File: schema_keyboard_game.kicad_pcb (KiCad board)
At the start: 2 copper layers, 228 parts, among them J1 USB_C_Receptacle_PowerOnly_6P, SW101 SW_Push, U1 ESP32-S3-DevKitC

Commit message: Add new layout, update schema
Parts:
- added J2: Conn_01x04, Connector_PinSocket_2.54mm:PinSocket_1x04_P2.54mm_Vertical, F.Cu at (382.3, 278.1)
- SW1, SW10, SW100, SW11, SW12, SW13, SW14, SW15, SW16, SW17, SW18, SW19, SW2, SW20, SW21, SW22, SW23, SW24, SW25, SW26, SW27, SW28, SW29, SW3, SW30, SW31, SW32, SW33, SW34, SW35, SW36, SW37, SW38, SW39, SW4, SW40, SW41, SW42, SW43, SW44, SW45, SW46, SW47, SW48, SW49, SW5, SW50, SW51, SW52, SW53, SW54, SW55, SW56, SW57, SW58, SW59, SW6, SW60, SW61, SW62, SW63, SW64, SW65, SW66, SW67, SW68, SW69, SW7, SW70, SW71, SW72, SW73, SW74, SW75, SW76, SW77, SW78, SW79, SW8, SW80, SW81, SW82, SW83, SW84, SW85, SW86, SW87, SW88, SW89, SW9, SW90, SW91, SW92, SW93, SW94, SW95, SW96, SW97, SW98, SW99: footprint Library:SW_Cherry_MX_LED -> Library:SW_Cherry_MX_LED_2
- moved SW99 30.4 mm to (232.9, 268.6)
- moved SW89 28.9 mm to (232.9, 249.4)
- moved SW79 27.6 mm to (232.9, 230.3)
- moved SW69 26.3 mm to (232.9, 211.2)
- moved SW59 25.1 mm to (232.9, 192.1)
- moved SW49 24.0 mm to (232.9, 172.9)
- moved SW80 23.9 mm to (252.7, 230.4)
- moved SW39 23.1 mm to (232.9, 153.8)
- moved SW70 22.4 mm to (252.7, 211.2)
- moved SW29 22.3 mm to (232.9, 134.7)
- moved SW19 21.7 mm to (232.9, 115.6)
- moved SW9 21.2 mm to (232.9, 96.4)
- moved SW60 21.0 mm to (252.7, 192.1)
- moved SW90 20.4 mm to (252.7, 249.5)
- moved SW50 19.7 mm to (252.7, 173.0)
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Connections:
- LCD1 pad 1: +3V3 -> GND
- LCD1 pad 2: (no net) -> +3V3

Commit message: New draft of pcb plate
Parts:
- moved SW6 123.6 mm to (34.3, 130.8)
- moved SW5 104.5 mm to (34.3, 110.5)
- moved SW21 98.8 mm to (74.9, 29.2)
- moved SW4 88.5 mm to (34.3, 90.2)
- moved SW11 85.6 mm to (54.6, 29.2)
- moved SW1 79.0 mm to (34.3, 29.2)
- moved SW3 77.6 mm to (34.3, 69.8)
- moved SW2 74.1 mm to (34.3, 49.5)
- moved SW12 8.03 mm to (95.0, 119.3)
- moved SW13 8.03 mm to (110.0, 119.3)
- moved SW22 8.03 mm to (95.0, 135.6)
- moved SW23 8.03 mm to (110.0, 135.6)
- moved SW31 8.03 mm to (79.9, 151.9)
- moved SW32 8.03 mm to (95.0, 151.9)
- moved SW33 8.03 mm to (110.0, 151.9)
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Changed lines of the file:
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@@
 	(footprint "Library:SW_Cherry_MX_LED_2"
 		(layer "F.Cu")
-		(at 77.32 176.825)
+		(at 79.86 184.445)
 		(descr "Cherry MX keyswitch, 1.00u, plate mount, http://cherryamericas.com/wp-content/uploads/2014/12/mx_cat.pdf")
 		(tags "Cherry MX keyswitch 1.00u plate")
@@
 	(footprint "Library:SW_Cherry_MX_LED_2"
 		(layer "F.Cu")
-		(at 92.41 209.375)
+		(at 94.95 216.995)
 		(descr "Cherry MX keyswitch, 1.00u, plate mount, http://cherryamericas.com/wp-content/uploads/2014/12/mx_cat.pdf")
 		(tags "Cherry MX keyswitch 1.00u plate")
@@
 	(footprint "Library:SW_Cherry_MX_LED_2"
 		(layer "F.Cu")
-		(at 92.41 225.65)
+		(at 94.95 233.27)
 		(descr "Cherry MX keyswitch, 1.00u, plate mount, http://cherryamericas.com/wp-content/uploads/2014/12/mx_cat.pdf")
 		(tags "Cherry MX keyswitch 1.00u plate")
@@
 	(footprint "Library:SW_Cherry_MX_LED_2"
 		(layer "F.Cu")
-		(at 107.5 209.375)
+		(at 110.04 216.995)
 		(descr "Cherry MX keyswitch, 1.00u, plate mount, http://cherryamericas.com/wp-content/uploads/2014/12/mx_cat.pdf")
 		(tags "Cherry MX keyswitch 1.00u plate")
@@
 	(footprint "Library:SW_Cherry_MX_LED_2"
 		(layer "F.Cu")
-		(at 77.32 225.65)
+		(at 79.86 233.27)
 		(descr "Cherry MX keyswitch, 1.00u, plate mount, http://cherryamericas.com/wp-content/uploads/2014/12/mx_cat.pdf")
 		(tags "Cherry MX keyswitch 1.00u plate")
@@
 	(footprint "Library:SW_Cherry_MX_LED_2"
 		(layer "F.Cu")
-		(at 92.41 111.725)
+		(at 94.95 119.345)
 		(descr "Cherry MX keyswitch, 1.00u, plate mount, http://cherryamericas.com/wp-content/uploads/2014/12/mx_cat.pdf")
 		(tags "Cherry MX keyswitch 1.00u plate")
@@
 	)
 	(footprint "Library:SW_Cherry_MX_LED_2"
+		(locked yes)
 		(layer "F.Cu")
-		(at 92.41 95.45)
+		(at 34.29 49.53)
 		(descr "Cherry MX keyswitch, 1.00u, plate mount, http://cherryamericas.com/wp-content/uploads/2014/12/mx_cat.pdf")
 		(tags "Cherry MX keyswitch 1.00u plate")
@@
 	(footprint "Library:SW_Cherry_MX_LED_2"
 		(layer "F.Cu")
-		(at 107.5 144.275)
+		(at 110.04 151.895)
 		(descr "Cherry MX keyswitch, 1.00u, plate mount, http://cherryamericas.com/wp-content/uploads/2014/12/mx_cat.pdf")
 		(tags "Cherry MX keyswitch 1.00u plate")
@@
 	(footprint "Library:SW_Cherry_MX_LED_2"
 		(layer "F.Cu")
-		(at 92.41 241.925)
+		(at 94.95 249.545)
 		(descr "Cherry MX keyswitch, 1.00u, plate mount, http://cherryamericas.com/wp-content/uploads/2014/12/mx_cat.pdf")
 		(tags "Cherry MX keyswitch 1.00u plate")
@@
 	(footprint "Library:SW_Cherry_MX_LED_2"
 		(layer "F.Cu")
-		(at 107.5 176.825)
+		(at 110.04 184.445)
 		(descr "Cherry MX keyswitch, 1.00u, plate mount, http://cherryamericas.com/wp-content/uploads/2014/12/mx_cat.pdf")
 		(tags "Cherry MX keyswitch 1.00u plate")
@@
 	(footprint "Library:SW_Cherry_MX_LED_2"
 		(layer "F.Cu")
-		(at 107.5 111.725)
+		(at 110.04 119.345)
 		(descr "Cherry MX keyswitch, 1.00u, plate mount, http://cherryamericas.com/wp-content/uploads/2014/12/mx_cat.pdf")
 		(tags "Cherry MX keyswitch 1.00u plate")
@@
 	)
 	(footprint "Library:SW_Cherry_MX_LED_2"
+		(locked yes)
 		(layer "F.Cu")
-		(at 77.32 128)
+		(at 74.93 29.21)
 		(descr "Cherry MX keyswitch, 1.00u, plate mount, http://cherryamericas.com/wp-content/uploads/2014/12/mx_cat.pdf")
 		(tags "Cherry MX keyswitch 1.00u plate")
@@
 	(footprint "Library:SW_Cherry_MX_LED_2"
 		(layer "F.Cu")
-		(at 107.5 193.1)
+		(at 110.04 200.72)
 		(descr "Cherry MX keyswitch, 1.00u, plate mount, http://cherryamericas.com/wp-content/uploads/2014/12/mx_cat.pdf")
 		(tags "Cherry MX keyswitch 1.00u plate")
@@
 	)
 	(footprint "Library:SW_Cherry_MX_LED_2"
+		(locked yes)
 		(layer "F.Cu")
-		(at 137.68 95.45)
+		(at 34.29 110.49)
 		(descr "Cherry MX keyswitch, 1.00u, plate mount, http://cherryamericas.com/wp-content/uploads/2014/12/mx_cat.pdf")
 		(tags "Cherry MX keyswitch 1.00u plate")
@@
 	)
 	(footprint "Library:SW_Cherry_MX_LED_2"
+		(locked yes)
 		(layer "F.Cu")
-		(at 107.5 95.45)
+		(at 34.29 69.85)
 		(descr "Cherry MX keyswitch, 1.00u, plate mount, http://cherryamericas.com/wp-content/uploads/2014/12/mx_cat.pdf")
 		(tags "Cherry MX keyswitch 1.00u plate")
@@
 	(footprint "Library:SW_Cherry_MX_LED_2"
 		(layer "F.Cu")
-		(at 77.32 160.55)
+		(at 79.86 168.17)
 		(descr "Cherry MX keyswitch, 1.00u, plate mount, http://cherryamericas.com/wp-content/uploads/2014/12/mx_cat.pdf")
 		(tags "Cherry MX keyswitch 1.00u plate")
@@
 	(footprint "Library:SW_Cherry_MX_LED_2"
 		(layer "F.Cu")
-		(at 77.32 193.1)
+		(at 79.86 200.72)
 		(descr "Cherry MX keyswitch, 1.00u, plate mount, http://cherryamericas.com/wp-content/uploads/2014/12/mx_cat.pdf")
 		(tags "Cherry MX keyswitch 1.00u plate")
@@
 	(footprint "Library:SW_Cherry_MX_LED_2"
 		(layer "F.Cu")
-		(at 92.41 160.55)
+		(at 94.95 168.17)
 		(descr "Cherry MX keyswitch, 1.00u, plate mount, http://cherryamericas.com/wp-content/uploads/2014/12/mx_cat.pdf")
 		(tags "Cherry MX keyswitch 1.00u plate")
@@
 	(footprint "Library:SW_Cherry_MX_LED_2"
 		(layer "F.Cu")
-		(at 92.41 176.825)
+		(at 94.95 184.445)
 		(descr "Cherry MX keyswitch, 1.00u, plate mount, http://cherryamericas.com/wp-content/uploads/2014/12/mx_cat.pdf")
 		(tags "Cherry MX keyswitch 1.00u plate")
@@
 	(footprint "Library:SW_Cherry_MX_LED_2"
 		(layer "F.Cu")
-		(at 107.5 241.925)
+		(at 110.04 249.545)
 		(descr "Cherry MX keyswitch, 1.00u, plate mount, http://cherryamericas.com/wp-content/uploads/2014/12/mx_cat.pdf")
 		(tags "Cherry MX keyswitch 1.00u plate")
@@
 	(footprint "Library:SW_Cherry_MX_LED_2"
 		(layer "F.Cu")
-		(at 107.5 160.55)
+		(at 110.04 168.17)
 		(descr "Cherry MX keyswitch, 1.00u, plate mount, http://cherryamericas.com/wp-content/uploads/2014/12/mx_cat.pdf")
 		(tags "Cherry MX keyswitch 1.00u plate")
@@
 	)
 	(footprint "Library:SW_Cherry_MX_LED_2"
+		(locked yes)
 		(layer "F.Cu")
-		(at 152.77 95.45)
+		(at 34.29 130.81)
 		(descr "Cherry MX keyswitch, 1.00u, plate mount, http://cherryamericas.com/wp-content/uploads/2014/12/mx_cat.pdf")
 		(tags "Cherry MX keyswitch 1.00u plate")
@@
 	(footprint "Library:SW_Cherry_MX_LED_2"
 		(layer "F.Cu")
-		(at 92.41 144.275)
+		(at 94.95 151.895)
 		(descr "Cherry MX keyswitch, 1.00u, plate mount, http://cherryamericas.com/wp-content/uploads/2014/12/mx_cat.pdf")
 		(tags "Cherry MX keyswitch 1.00u plate")
@@
 	(footprint "Library:SW_Cherry_MX_LED_2"
 		(layer "F.Cu")
-		(at 77.32 144.275)
+		(at 79.86 151.895)
 		(descr "Cherry MX keyswitch, 1.00u, plate mount, http://cherryamericas.com/wp-content/uploads/2014/12/mx_cat.pdf")
 		(tags "Cherry MX keyswitch 1.00u plate")
@@
 	)
 	(footprint "Library:SW_Cherry_MX_LED_2"
+		(locked yes)
 		(layer "F.Cu")
-		(at 122.59 95.45)
+		(at 34.29 90.17)
 		(descr "Cherry MX keyswitch, 1.00u, plate mount, http://cherryamericas.com/wp-content/uploads/2014/12/mx_cat.pdf")
 		(tags "Cherry MX keyswitch 1.00u plate")
@@
 	(footprint "Library:SW_Cherry_MX_LED_2"
 		(layer "F.Cu")
-		(at 92.41 128)
+		(at 94.95 135.62)
 		(descr "Cherry MX keyswitch, 1.00u, plate mount, http://cherryamericas.com/wp-content/uploads/2014/12/mx_cat.pdf")
 		(tags "Cherry MX keyswitch 1.00u plate")
@@
 	(footprint "Library:SW_Cherry_MX_LED_2"
 		(layer "F.Cu")
-		(at 107.5 128)
+		(at 110.04 135.62)
 		(descr "Cherry MX keyswitch, 1.00u, plate mount, http://cherryamericas.com/wp-content/uploads/2014/12/mx_cat.pdf")
 		(tags "Cherry MX keyswitch 1.00u plate")
@@
 	(footprint "Library:SW_Cherry_MX_LED_2"
 		(layer "F.Cu")
-		(at 107.5 225.65)
+		(at 110.04 233.27)
 		(descr "Cherry MX keyswitch, 1.00u, plate mount, http://cherryamericas.com/wp-content/uploads/2014/12/mx_cat.pdf")
 		(tags "Cherry MX keyswitch 1.00u plate")
@@
 	(footprint "Library:SW_Cherry_MX_LED_2"
 		(layer "F.Cu")
-		(at 92.41 193.1)
+		(at 94.95 200.72)
 		(descr "Cherry MX keyswitch, 1.00u, plate mount, http://cherryamericas.com/wp-content/uploads/2014/12/mx_cat.pdf")
 		(tags "Cherry MX keyswitch 1.00u plate")
@@
 	)
 	(footprint "Library:SW_Cherry_MX_LED_2"
+		(locked yes)
 		(layer "F.Cu")
-		(at 77.32 111.725)
+		(at 54.61 29.21)
 		(descr "Cherry MX keyswitch, 1.00u, plate mount, http://cherryamericas.com/wp-content/uploads/2014/12/mx_cat.pdf")
 		(tags "Cherry MX keyswitch 1.00u plate")
@@
 	)
 	(footprint "Library:SW_Cherry_MX_LED_2"
+		(locked yes)
 		(layer "F.Cu")
-		(at 77.32 95.45)
+		(at 34.29 29.21)
 		(descr "Cherry MX keyswitch, 1.00u, plate mount, http://cherryamericas.com/wp-content/uploads/2014/12/mx_cat.pdf")
 		(tags "Cherry MX keyswitch 1.00u plate")
@@
 	(footprint "Library:SW_Cherry_MX_LED_2"
 		(layer "F.Cu")
-		(at 77.32 241.925)
+		(at 79.86 249.545)
 		(descr "Cherry MX keyswitch, 1.00u, plate mount, http://cherryamericas.com/wp-content/uploads/2014/12/mx_cat.pdf")
 		(tags "Cherry MX keyswitch 1.00u plate")
@@
 	(footprint "Library:SW_Cherry_MX_LED_2"
 		(layer "F.Cu")
-		(at 77.32 209.375)
+		(at 79.86 216.995)
 		(descr "Cherry MX keyswitch, 1.00u, plate mount, http://cherryamericas.com/wp-content/uploads/2014/12/mx_cat.pdf")
 		(tags "Cherry MX keyswitch 1.00u plate")

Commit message: Keys are on the right place
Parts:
- moved SW91 259.6 mm to (217.2, 29.2)
- moved SW10 247.1 mm to (34.3, 212.1)
- moved SW81 235.2 mm to (196.8, 29.2)
- moved SW92 234.4 mm to (217.2, 49.5)
- moved SW20 220.5 mm to (54.5, 212.1)
- moved SW9 220.3 mm to (34.3, 191.8)
- moved SW71 211.2 mm to (176.5, 29.2)
- moved SW82 210.1 mm to (196.8, 49.5)
- moved SW93 209.2 mm to (217.2, 69.8)
- moved SW19 193.9 mm to (54.6, 191.8)
- moved SW30 193.9 mm to (74.9, 212.1)
- moved SW61 187.7 mm to (156.2, 29.2)
- moved SW72 186.3 mm to (176.5, 49.5)
- moved SW83 185.0 mm to (196.8, 69.8)
- moved SW94 178.8 mm to (217.2, 90.2)
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
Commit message: PCB ver 1.0
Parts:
- C1, C10, C100, C101, C11, C12, C13, C14, C15, C16, C17, C18, C19, C2, C20, C21, C22, C23, C24, C25, C26, C27, C28, C29, C3, C30, C31, C32, C33, C34, C35, C36, C37, C38, C39, C4, C40, C41, C42, C43, C44, C45, C46, C47, C48, C49, C5, C50, C51, C52, C53, C54, C55, C56, C57, C58, C59, C6, C60, C61, C62, C63, C64, C65, C66, C67, C68, C69, C7, C70, C71, C72, C73, C74, C75, C76, C77, C78, C79, C8, C80, C81, C82, C83, C84, C85, C86, C87, C88, C89, C9, C90, C91, C92, C93, C94, C95, C96, C97, C98, C99, D1, D10, D2, D3, D4, D5, D6, D7, D8, D9, R1, R10, R11, R12, R13, R4, R5, R6, R7, R8, R9: moved to B.Cu
- moved D6 410.1 mm to (92.7, 51.2), turned to -90 degrees
- moved D8 398.4 mm to (113.0, 43.2), turned to -90 degrees
- moved D7 384.0 mm to (113.0, 72.8), turned to -90 degrees
- moved D9 382.2 mm to (133.3, 43.2), turned to -90 degrees
- moved C71 377.2 mm to (82.5, 223.5)
- moved C1 370.6 mm to (82.3, 44.5)
- moved D10 366.5 mm to (153.7, 43.2), turned to -90 degrees
- moved C2 365.9 mm to (82.3, 64.8)
- moved C10 361.9 mm to (102.9, 44.5)
- moved C3 361.6 mm to (82.5, 85.1)
- moved C4 358.4 mm to (82.5, 105.4)
- moved C42 356.3 mm to (123.2, 44.5)
- moved C5 355.9 mm to (82.5, 125.7)
- moved C11 355.5 mm to (102.9, 64.8)
- moved C6 354.2 mm to (82.5, 146.1)
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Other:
- board outline added: 240 x 208.3 mm

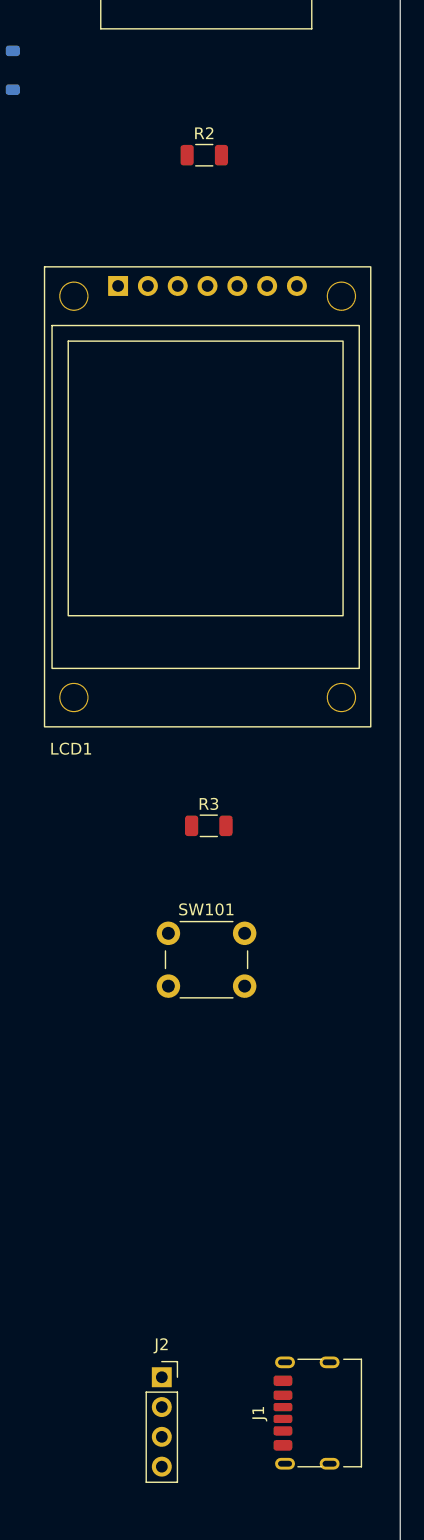
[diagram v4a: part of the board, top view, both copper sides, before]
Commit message: Update schema with new out pins
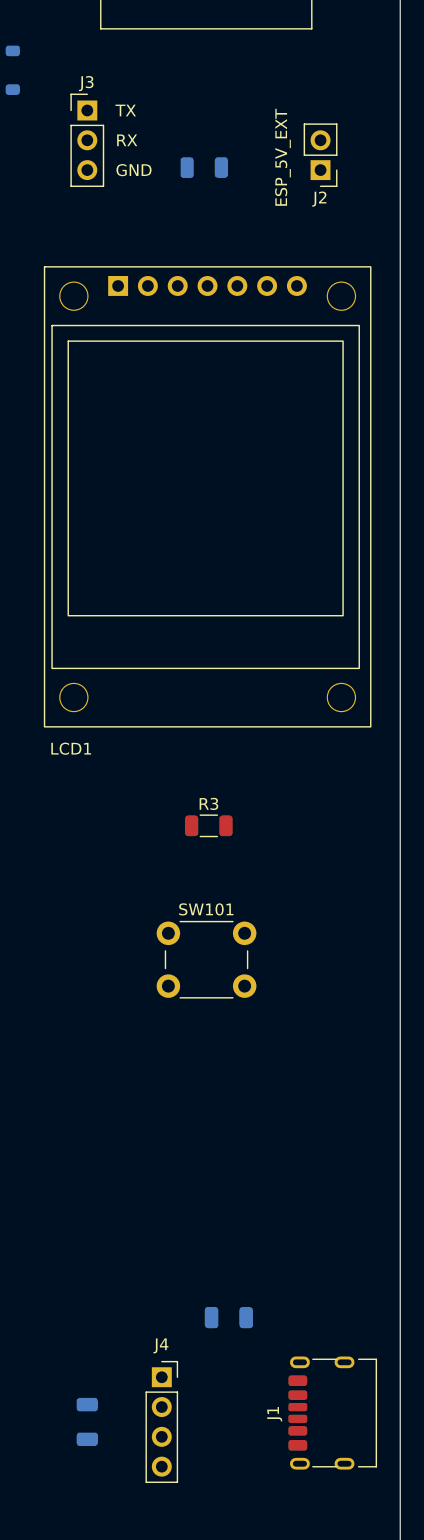
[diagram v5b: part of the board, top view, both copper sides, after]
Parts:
- added C102: C, Capacitor_SMD:C_1206_3216Metric, B.Cu at (294.0, 203.2)
- added C103: C, Capacitor_SMD:C_1206_3216Metric, B.Cu at (281.9, 212.1)
- added J2: Conn_01x02, Connector_PinHeader_2.54mm:PinHeader_1x02_P2.54mm_Vertical, F.Cu at (301.8, 105.4)
- added J3: Conn_01x03, Connector_PinHeader_2.54mm:PinHeader_1x03_P2.54mm_Vertical, F.Cu at (281.9, 100.3)
- R2: moved to B.Cu
- moved J1 1.27 mm to (303.1, 211.3)
- moved R2 1.06 mm to (291.9, 105.2)
- renumbered J2 to J4
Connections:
- U1 pad 21: +5V -> /esp_5V_external
- U1 pad 42: unconnected-(U1-GPIO44/U0RXD-Pad42) -> /uart_rx
- U1 pad 43: unconnected-(U1-GPIO43/U0TXD-Pad43) -> /uart_tx
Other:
- board text added: "ESP_5V_EXT"
- board text added: "GND"
- board text added: "RX"
- board text added: "TX"

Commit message: PCB ver 1.1
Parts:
- moved SW101 7.64 mm to (295.4, 174.5), turned to 180 degrees
- moved J1 1.34 mm to (304.3, 211.8)
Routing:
- net +5V: track 0.00 -> 3284.0 mm, vias 0 -> 103
- net /cl_10: track 0.00 -> 276.8 mm
- net Net-(D6-K): track 0.00 -> 249.1 mm
- net /cl_2: track 0.00 -> 241.0 mm
- net /cl_9: track 0.00 -> 225.7 mm, vias 0 -> 4
- net Net-(D8-K): track 0.00 -> 225.0 mm
- net /cl_1: track 0.00 -> 222.6 mm
- net /cl_8: track 0.00 -> 221.0 mm, vias 0 -> 3
- net /led_1: track 0.00 -> 205.4 mm
- net Net-(U1-GPIO10/ADC1_CH9): track 0.00 -> 200.5 mm, vias 0 -> 1
- net /cl_6: track 0.00 -> 197.7 mm
- net /cl_7: track 0.00 -> 197.2 mm
- net /row_7: track 0.00 -> 193.7 mm, vias 0 -> 1
- net /row_10: track 0.00 -> 193.2 mm
- net /row_8: track 0.00 -> 193.2 mm
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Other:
- board text added: "+3V"
- board text added: "+5V"

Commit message: Add TTL logic, update schema and pcb, draft
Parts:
- added C104: C, Capacitor_SMD:C_1206_3216Metric, F.Cu at (280.7, 37.5)
- added R14: 470, Resistor_SMD:R_1206_3216Metric, B.Cu at (255.3, 176.5)
- added R15: 470, Resistor_SMD:R_1206_3216Metric, B.Cu at (255.3, 196.8)
- added R16: 470, Resistor_SMD:R_1206_3216Metric, B.Cu at (255.3, 217.2)
- added U2: ESP32-S3-DevKitC, Espressif:ESP32-S3-DevKit_ALI, F.Cu at (280.0, 162.6)
- C101, C103, D3, R1, R2, R4, R5, R6: moved to F.Cu
- C102: value C -> 100p; moved to F.Cu
- U1: value ESP32-S3-DevKitC -> 74AHCT125; footprint Espressif:ESP32-S3-DevKit_ALI -> Package_DIP:DIP-14_W7.62mm
- moved C103 184.0 mm to (295.1, 28.6), turned to 180 degrees
- moved C90 183.1 mm to (265.4, 105.5), turned to 0 degrees
- moved D10 175.2 mm to (174.0, 217.2), turned to 90 degrees
- moved D8 175.2 mm to (133.3, 217.2), turned to 90 degrees
- moved D9 175.2 mm to (153.7, 217.2), turned to 90 degrees
- moved J1 174.3 mm to (303.9, 37.5)
- moved J4 174.3 mm to (287.8, 34.0)
- moved D6 166.0 mm to (92.7, 217.2), turned to 90 degrees
- moved C102 154.8 mm to (291.7, 48.4), turned to 0 degrees
- moved D5 145.7 mm to (214.6, 217.2), turned to 90 degrees
- moved D7 144.4 mm to (113.0, 217.2), turned to 90 degrees
- moved D1 142.2 mm to (234.9, 217.2), turned to 90 degrees
- moved D4 124.1 mm to (194.3, 217.2), turned to 90 degrees
- moved R1 106.7 mm to (280.7, 65.8), turned to -90 degrees
- moved R3 103.3 mm to (280.7, 58.7), turned to -90 degrees
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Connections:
- C103 pad 1: +3V3 -> GND
- C103 pad 2: GND -> +5V
- R1 pad 2: Net-(U1-GPIO39/MTCK) -> Net-(U2-GPIO39/MTCK)
- R10 pad 1: Net-(U1-GPIO7/ADC1_CH6) -> Net-(U2-GPIO4/ADC1_CH3)
- R10 pad 2: /row_7 -> /row_4
- R11 pad 1: Net-(U1-GPIO8/ADC1_CH7) -> Net-(U2-GPIO5/ADC1_CH4)
- R11 pad 2: /row_8 -> /row_5
- R12 pad 1: Net-(U1-GPIO9/ADC1_CH8) -> Net-(U2-GPIO6/ADC1_CH5)
- R12 pad 2: /row_9 -> /row_6
- R13 pad 1: Net-(U1-GPIO10/ADC1_CH9) -> Net-(U2-GPIO7/ADC1_CH6)
- R13 pad 2: /row_10 -> /row_7
- R3 pad 1: Net-(R3-Pad1) -> +5V
- R3 pad 2: /key_1 -> Net-(R3-Pad2)
- R4 pad 1: Net-(U1-GPIO1/ADC1_CH0) -> +5V
- R4 pad 2: /row_1 -> Net-(R4-Pad2)
- R5 pad 1: Net-(U1-GPIO2/ADC1_CH1) -> Net-(R5-Pad1)
- R5 pad 2: /row_2 -> /key_1
- R6 pad 1: Net-(U1-GPIO3/ADC1_CH2) -> +5V
- R6 pad 2: /row_3 -> Net-(R6-Pad2)
- R7 pad 1: Net-(U1-GPIO4/ADC1_CH3) -> Net-(U2-GPIO1/ADC1_CH0)
- R7 pad 2: /row_4 -> /row_1
- R8 pad 1: Net-(U1-GPIO5/ADC1_CH4) -> Net-(U2-GPIO2/ADC1_CH1)
- R8 pad 2: /row_5 -> /row_2
- R9 pad 1: Net-(U1-GPIO6/ADC1_CH5) -> Net-(U2-GPIO3/ADC1_CH2)
- R9 pad 2: /row_6 -> /row_3
- SW1 pad 4: /rgb_in -> /rgb_in_5V
- SW101 pad 2: Net-(R3-Pad1) -> Net-(R5-Pad1)
- U1 pad 1: +3V3 -> GND
- U1 pad 10: Net-(D7-K) -> Net-(R4-Pad2)
- U1 pad 11: Net-(D8-K) -> unconnected-(U1-Pad11)
- U1 pad 12: Net-(U1-GPIO8/ADC1_CH7) -> Net-(R6-Pad2)
- U1 pad 13: Net-(U1-GPIO3/ADC1_CH2) -> Net-(R6-Pad2)
- U1 pad 14: unconnected-(U1-GPIO46-Pad14) -> +5V
- U1 pad 2: +3V3 -> /rgb_in
- U1 pad 3: unconnected-(U1-RESET-Pad3) -> /rgb_in_5V
- U1 pad 4: Net-(U1-GPIO4/ADC1_CH3) -> Net-(R3-Pad2)
- U1 pad 5: Net-(U1-GPIO5/ADC1_CH4) -> Net-(R3-Pad2)
- U1 pad 6: Net-(U1-GPIO6/ADC1_CH5) -> unconnected-(U1-Pad6)
- U1 pad 7: Net-(U1-GPIO7/ADC1_CH6) -> GND
- U1 pad 8: Net-(D4-K) -> unconnected-(U1-Pad8)
- U1 pad 9: Net-(D5-K) -> Net-(R4-Pad2)
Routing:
- net +5V: track 3284.0 -> 3004.4 mm, vias 103 -> 100
- net /cl_10: track 276.8 -> 0.00 mm
- net Net-(D6-K): track 249.1 -> 0.00 mm
- net /cl_2: track 241.0 -> 0.00 mm
- net /cl_9: track 225.7 -> 0.00 mm, vias 4 -> 0
- net Net-(D8-K): track 225.0 -> 0.00 mm
- net /cl_1: track 222.6 -> 0.00 mm
- net /cl_8: track 221.0 -> 0.00 mm, vias 3 -> 0
- net /led_1: track 205.4 -> 0.00 mm
- net Net-(U1-GPIO10/ADC1_CH9): track 200.5 -> 0.00 mm, vias 1 -> 0
- net /cl_6: track 197.7 -> 0.00 mm
- net /cl_7: track 197.2 -> 0.00 mm
- net /row_7: track 193.7 -> 0.00 mm, vias 1 -> 0
- net /row_10: track 193.2 -> 0.00 mm
- net /row_8: track 193.2 -> 0.00 mm
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
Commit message: Schema and PCB, ver 1.5
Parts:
- added C105: 100p, Capacitor_SMD:C_1206_3216Metric, F.Cu at (292.1, 152.2)
- added R17: 4.7 K, Resistor_SMD:R_1206_3216Metric, B.Cu at (293.7, 78.4)
- added R18: 4.7 K, Resistor_SMD:R_1206_3216Metric, B.Cu at (290.4, 78.4)
- moved D2 110.1 mm to (234.9, 193.3), turned to 90 degrees
- moved R12 7.62 mm to (255.3, 128.3), turned to -90 degrees
- moved R16 7.56 mm to (255.3, 209.6), turned to -90 degrees
- moved R10 3.81 mm to (255.3, 91.6)
- moved R14 3.62 mm to (255.4, 172.9)
- moved R13 3.62 mm to (255.3, 152.6)
- moved R15 3.62 mm to (255.3, 193.2)
- moved R9 3.62 mm to (255.3, 71.3)
- moved R7 3.62 mm to (255.3, 30.7)
- moved R11 3.62 mm to (255.3, 112.0)
- moved R8 3.56 mm to (255.3, 51.1), turned to 90 degrees
- moved D1 3.43 mm to (234.9, 213.7)
- moved D10 3.43 mm to (174.0, 213.7)
- moved D4 3.43 mm to (194.3, 213.7)
- moved D5 3.43 mm to (214.6, 213.7)
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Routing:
- net /cl_10: track 0.00 -> 292.1 mm, vias 0 -> 2
- net GND: track 0.00 -> 244.9 mm
- net /cl_8: track 0.00 -> 217.4 mm, vias 0 -> 8
- net /cl_7: track 0.00 -> 216.2 mm, vias 0 -> 8
- net /cl_2: track 0.00 -> 215.2 mm, vias 0 -> 8
- net /cl_6: track 0.00 -> 214.3 mm, vias 0 -> 8
- net /cl_4: track 0.00 -> 214.0 mm, vias 0 -> 8
- net /cl_5: track 0.00 -> 213.6 mm, vias 0 -> 8
- net /cl_3: track 0.00 -> 212.5 mm, vias 0 -> 8
- net Net-(D7-K): track 0.00 -> 208.6 mm, vias 0 -> 1
- net /cl_9: track 0.00 -> 203.6 mm, vias 0 -> 8
- net /cl_1: track 0.00 -> 197.9 mm
- net /led_1: track 0.00 -> 192.5 mm, vias 0 -> 2
- net Net-(D6-K): track 0.00 -> 190.8 mm, vias 0 -> 1
- net /row_6: track 0.00 -> 183.8 mm
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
